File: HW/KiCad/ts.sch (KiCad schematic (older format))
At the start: 45 parts, among them J1 AVR-ISP-6, J2 Conn_01x04, J3 Conn_01x04, J4 Conn_01x07, J5 Conn_01x04, J6 Conn_01x08, Q1 IRFZ24N, Q2 IRFZ24N, U1 ATmega328P-PU, U2 LM2576HVT-5, U3 HT7533, U4 LM75C, U5 4050, X1 Screw_Terminal_01x02, X2 Screw_Terminal_01x02, Y1 20MHz

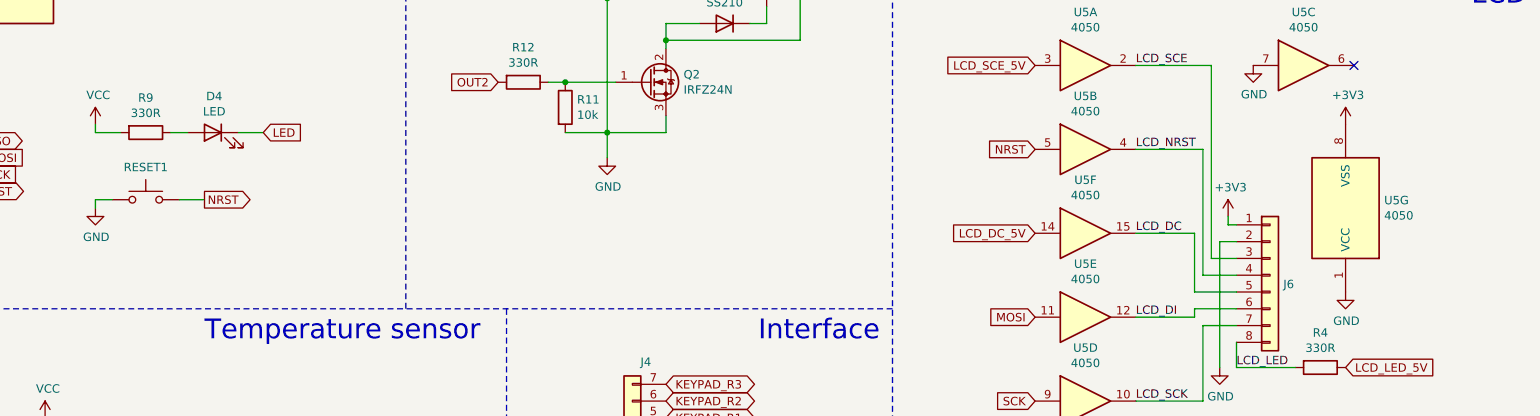
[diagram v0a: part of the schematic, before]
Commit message: [HW] Fixed issues in the KiCad schematics
Fixed some footprints associations, 4050 buffer power supply.
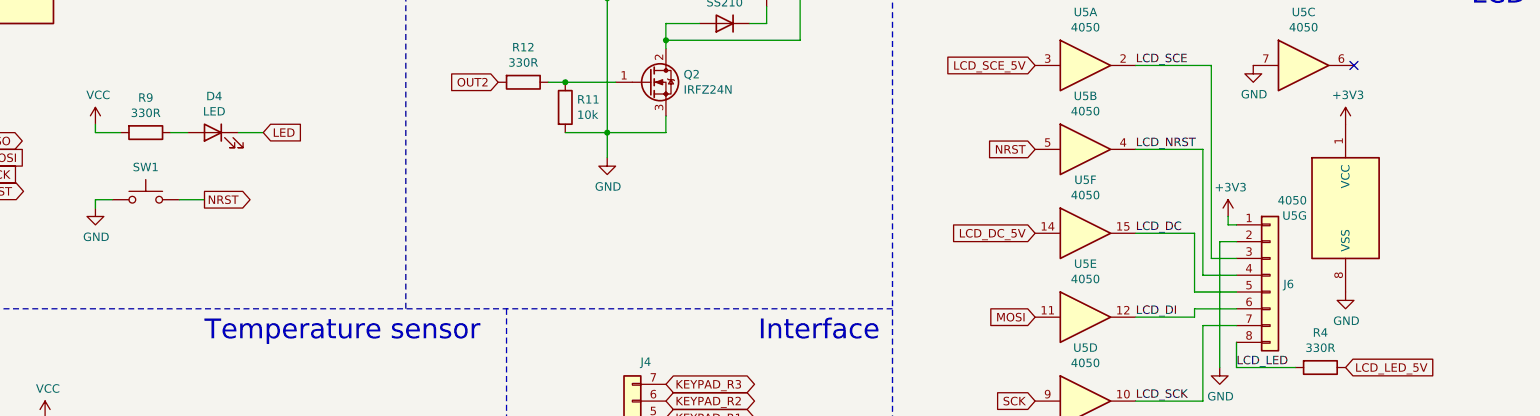
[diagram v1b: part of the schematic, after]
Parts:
- D1: footprint Diode_THT:D_5W_P10.16mm_Horizontal -> Diode_THT:D_DO-201AD_P15.24mm_Horizontal
- L1: footprint Inductor_THT:L_Toroid_Vertical_L13.0mm_W6.5mm_P5.60mm -> Inductor_THT:L_Toroid_Vertical_L16.4mm_W7.6mm_P6.60mm_Vishay_TJ3
- renumbered RESET1 to SW1
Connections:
- net +3V3: now also U5.1 (VCC); no longer U5.8 (VSS)
- net GND: now also U5.8 (VSS); no longer U5.1 (VCC)
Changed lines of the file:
@@
 	3650 4550 3500 4550
 $Comp
-L Switch:SW_Push RESET1
+L Switch:SW_Push SW1
 U 1 1 5C159D8B
 P 2950 4950
-F 0 "RESET1" H 2950 5143 50  0000 C CNN
+F 0 "SW1" H 2950 5143 50  0000 C CNN
 F 1 "RESET" H 2950 5144 50  0001 C CNN
 F 2 "Button_Switch_THT:SW_PUSH_6mm" H 2950 5150 50  0001 C CNN
@@
 F 3 "http://www.intersil.com/content/dam/intersil/documents/cd40/cd4050bms.pdf" H 10100 5000 50  0001 C CNN
 	7    10100 5000
-	-1   0    0    1
+	1    0    0    -1
 $EndComp
 Text GLabel 8250 4150 0    50   Input ~ 0
@@
 F 0 "D1" V 10504 1629 50  0000 L CNN
 F 1 "1N5820" V 10595 1629 50  0000 L CNN
-F 2 "Diode_THT:D_5W_P10.16mm_Horizontal" H 10550 1375 50  0001 C CNN
+F 2 "Diode_THT:D_DO-201AD_P15.24mm_Horizontal" H 10550 1375 50  0001 C CNN
 F 3 "http://www.vishay.com/docs/88526/1n5820.pdf" H 10550 1550 50  0001 C CNN
 	1    10550 1550
@@
 F 0 "L1" H 10253 1596 50  0000 L CNN
 F 1 "100uH" H 10253 1505 50  0000 L CNN
-F 2 "Inductor_THT:L_Toroid_Vertical_L13.0mm_W6.5mm_P5.60mm" H 10200 1550 50  0001 C CNN
+F 2 "Inductor_THT:L_Toroid_Vertical_L16.4mm_W7.6mm_P6.60mm_Vishay_TJ3" H 10200 1550 50  0001 C CNN
 F 3 "~" H 10200 1550 50  0001 C CNN
 	1    10200 1550

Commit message: [HW] Place KiCad layout components
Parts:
- J1: symbol Connector:AVR-ISP-6 -> ts-rescue:AVR-ISP-6-Connector
- Q1, Q2: value IRFZ24N -> IRLZ34N
- U1: symbol MCU_Microchip_ATmega:ATmega328P-PU -> ts-rescue:ATmega328P-PU-MCU_Microchip_ATmega
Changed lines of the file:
@@
 EESchema Schematic File Version 4
-LIBS:ts-cache
-EELAYER 26 0
+EELAYER 30 0
 EELAYER END
 $Descr A4 11693 8268
@@
 $EndDescr
 $Comp
-L MCU_Microchip_ATmega:ATmega328P-PU U1
+L ts-rescue:ATmega328P-PU-MCU_Microchip_ATmega U1
 U 1 1 5C141EF2
 P 1900 2500
@@
 Connection ~ 8600 1750
 $Comp
-L Connector:AVR-ISP-6 J1
+L ts-rescue:AVR-ISP-6-Connector J1
 U 1 1 5C357C61
 P 1550 4800
@@
 P 5950 3450
 F 0 "Q1" H 6155 3496 50  0000 L CNN
-F 1 "IRFZ24N" H 6155 3405 50  0000 L CNN
+F 1 "IRLZ34N" H 6155 3405 50  0000 L CNN
 F 2 "Package_TO_SOT_THT:TO-220-3_Vertical" H 6150 3550 50  0001 C CNN
 F 3 "~" H 5950 3450 50  0001 C CNN
@@
 P 5950 4250
 F 0 "Q2" H 6155 4296 50  0000 L CNN
-F 1 "IRFZ24N" H 6155 4205 50  0000 L CNN
+F 1 "IRLZ34N" H 6155 4205 50  0000 L CNN
 F 2 "Package_TO_SOT_THT:TO-220-3_Vertical" H 6150 4350 50  0001 C CNN
 F 3 "~" H 5950 4250 50  0001 C CNN
